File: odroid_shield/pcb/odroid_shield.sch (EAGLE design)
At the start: 70 parts, among them J1 AVRISP6_COMPACT, J4 ODROID_J4, U1 SINGLE-BIT_BUS_TRANSCEIVER, U10 ABM8G, U2 SINGLE-BIT_BUS_TRANSCEIVER, U3 ST1S10, U4 ATMEGA644P-20AU, U5 TS5205, U6 TCA9517MSOP8, U7 MP33926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

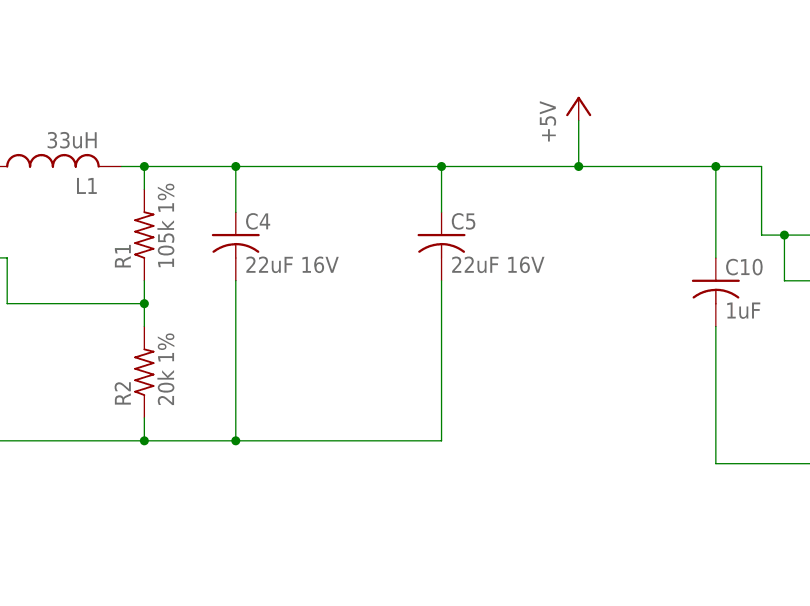
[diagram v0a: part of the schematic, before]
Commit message: odroid_shield: Preliminary routing of 5V regulator.
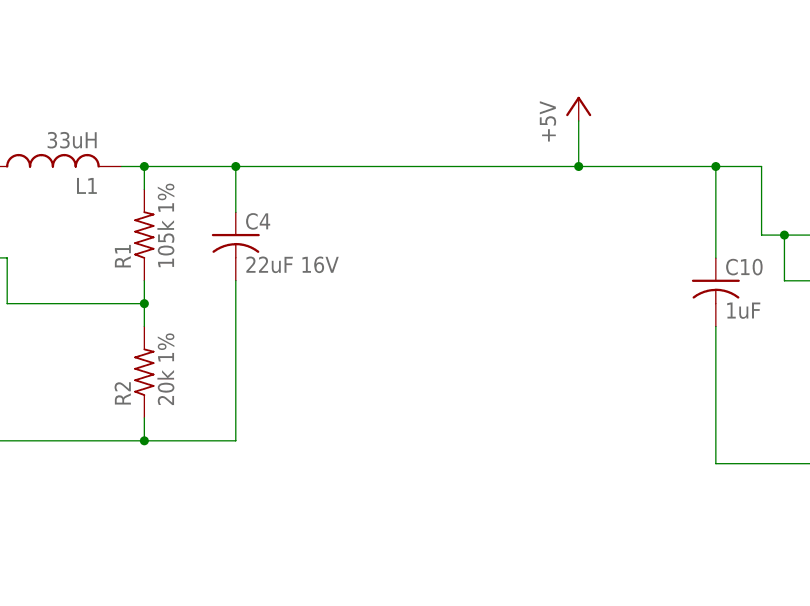
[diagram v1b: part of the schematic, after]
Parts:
- removed C5: 22uF 16V, rcl:C-USC1206
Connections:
- net +5V: no longer C5.1
- net GND: no longer C5.2
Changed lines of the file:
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@@
-<attribute name="DPN" value="445-3955-1-ND"/>
-</part>
-<part name="C5" library="rcl" deviceset="C-US" device="C1206" value="22uF 16V">
 <attribute name="DPN" value="445-3955-1-ND"/>
 </part>
@@
 <attribute name="DPN" x="220.98" y="-76.2" size="1.778" layer="96" display="off"/>
 </instance>
-<instance part="C5" gate="G$1" x="243.84" y="-76.2">
-<attribute name="DPN" x="243.84" y="-76.2" size="1.778" layer="96" display="off"/>
-</instance>
 <instance part="L1" gate="G$1" x="200.66" y="-68.58" rot="R90">
 <attribute name="DPN" x="200.66" y="-68.58" size="1.778" layer="96" rot="R90" display="off"/>
@@
 <wire x1="210.82" y1="-68.58" x2="220.98" y2="-68.58" width="0.1524" layer="91"/>
 <wire x1="220.98" y1="-68.58" x2="220.98" y2="-73.66" width="0.1524" layer="91"/>
-<wire x1="220.98" y1="-68.58" x2="243.84" y2="-68.58" width="0.1524" layer="91"/>
+<wire x1="220.98" y1="-68.58" x2="259.08" y2="-68.58" width="0.1524" layer="91"/>
 <junction x="220.98" y="-68.58"/>
-<pinref part="C5" gate="G$1" pin="1"/>
-<wire x1="243.84" y1="-68.58" x2="243.84" y2="-73.66" width="0.1524" layer="91"/>
 <pinref part="R1" gate="G$1" pin="2"/>
 <wire x1="210.82" y1="-68.58" x2="210.82" y2="-71.12" width="0.1524" layer="91"/>
 <junction x="210.82" y="-68.58"/>
 <pinref part="P+4" gate="1" pin="+5V"/>
-<wire x1="243.84" y1="-68.58" x2="259.08" y2="-68.58" width="0.1524" layer="91"/>
 <wire x1="259.08" y1="-68.58" x2="259.08" y2="-63.5" width="0.1524" layer="91"/>
-<junction x="243.84" y="-68.58"/>
 <wire x1="259.08" y1="-68.58" x2="274.32" y2="-68.58" width="0.1524" layer="91"/>
 <wire x1="274.32" y1="-68.58" x2="279.4" y2="-68.58" width="0.1524" layer="91"/>
@@
 <wire x1="220.98" y1="-99.06" x2="220.98" y2="-81.28" width="0.1524" layer="91"/>
 <junction x="180.34" y="-99.06"/>
-<pinref part="C5" gate="G$1" pin="2"/>
-<wire x1="220.98" y1="-99.06" x2="243.84" y2="-99.06" width="0.1524" layer="91"/>
-<wire x1="243.84" y1="-99.06" x2="243.84" y2="-81.28" width="0.1524" layer="91"/>
-<junction x="220.98" y="-99.06"/>
 <pinref part="R2" gate="G$1" pin="1"/>
 <wire x1="210.82" y1="-96.52" x2="210.82" y2="-99.06" width="0.1524" layer="91"/>
